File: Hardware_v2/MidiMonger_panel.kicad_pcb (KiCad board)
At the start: 2 copper layers, 40.3 x 128.5 mm, 32 parts

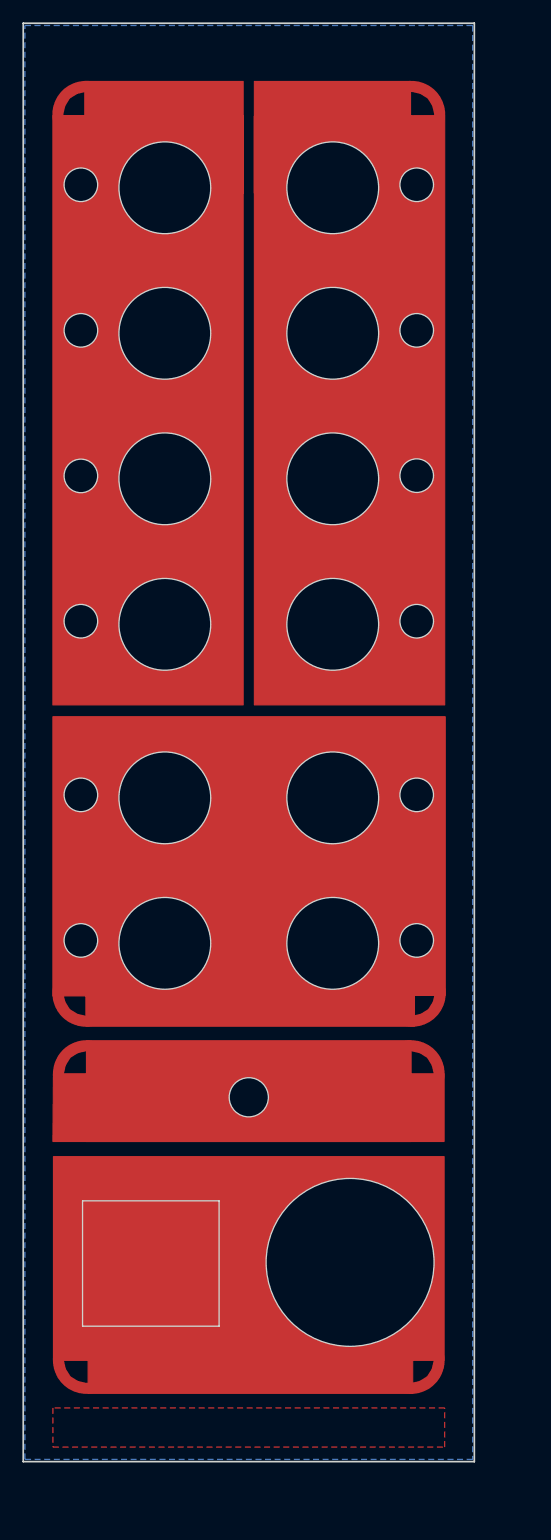
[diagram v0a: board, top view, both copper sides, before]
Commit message: Laying out panel
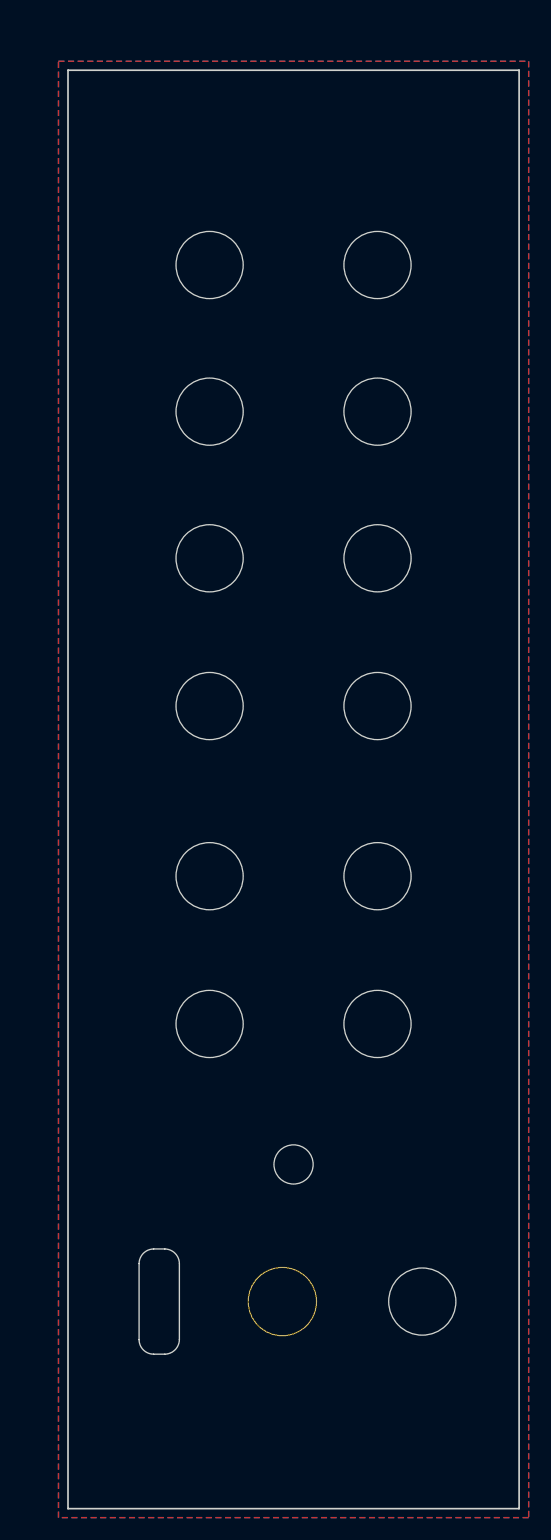
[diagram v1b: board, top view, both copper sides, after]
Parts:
- removed the Ref** at (123.5, 58.5)
- removed the Ref** at (123.5, 71.5)
- removed the Ref** at (123.5, 84.5)
- removed the Ref** at (123.5, 100.0)
- removed the Ref** at (123.5, 113.0)
- removed the Ref** at (108.5, 113.0)
- removed the Ref** at (108.5, 100.0)
- removed the Ref** at (108.5, 84.5)
- removed the Ref** at (108.5, 71.5)
- removed the Ref** at (108.5, 58.5)
- removed the Ref** at (108.5, 45.5)
- removed the Ref** at (123.5, 45.5)
- removed the Ref** at (125.0, 141.5)
- added REF**: USB_C_Cutout, Custom_Footprints:USB_C_Cutout, F.Cu at (108.0, 145.0)
- added Ref**: Thonkiconn_Socket_MountingHole_6mm, Custom_Footprints:Thonkiconn_Socket_MountingHole_6mm, F.Cu at (112.5, 52.4)
- added Ref**: Thonkiconn_Socket_MountingHole_6mm, Custom_Footprints:Thonkiconn_Socket_MountingHole_6mm, F.Cu at (112.5, 91.8)
- added Ref**: Thonkiconn_Socket_MountingHole_6mm, Custom_Footprints:Thonkiconn_Socket_MountingHole_6mm, F.Cu at (127.5, 78.6)
- added Ref**: Thonkiconn_Socket_MountingHole_6mm, Custom_Footprints:Thonkiconn_Socket_MountingHole_6mm, F.Cu at (127.5, 107.0)
- added Ref**: Thonkiconn_Socket_MountingHole_6mm, Custom_Footprints:Thonkiconn_Socket_MountingHole_6mm, F.Cu at (127.5, 65.5)
- added Ref**: Thonkiconn_Socket_MountingHole_6mm, Custom_Footprints:Thonkiconn_Socket_MountingHole_6mm, F.Cu at (127.5, 91.8)
- added Ref**: Thonkiconn_Socket_MountingHole_6mm, Custom_Footprints:Thonkiconn_Socket_MountingHole_6mm, F.Cu at (112.5, 78.6)
- added Ref**: Thonkiconn_Socket_MountingHole_6mm, Custom_Footprints:Thonkiconn_Socket_MountingHole_6mm, F.Cu at (131.5, 145.0)
- added Ref**: Thonkiconn_Socket_MountingHole_6mm, Custom_Footprints:Thonkiconn_Socket_MountingHole_6mm, F.Cu at (127.5, 120.2)
- added Ref**: Thonkiconn_Socket_MountingHole_6mm, Custom_Footprints:Thonkiconn_Socket_MountingHole_6mm, F.Cu at (112.5, 65.5)
- added Ref**: Subminiature_Switch, Custom_Footprints:DPDT_Switch_MountingHole_6mm, F.Cu at (119.0, 145.0)
- added Ref**: Thonkiconn_Socket_MountingHole_6mm, Custom_Footprints:Thonkiconn_Socket_MountingHole_6mm, F.Cu at (112.5, 107.0)
- added Ref**: Thonkiconn_Socket_MountingHole_6mm, Custom_Footprints:Thonkiconn_Socket_MountingHole_6mm, F.Cu at (127.5, 52.4)
- added Ref**: Thonkiconn_Socket_MountingHole_6mm, Custom_Footprints:Thonkiconn_Socket_MountingHole_6mm, F.Cu at (112.5, 120.2)
- added kibuzzard-66B25140: G***, kibuzzard-66B25140, F.Cu at (119.9, 113.6)
- added kibuzzard-66B25216: G***, kibuzzard-66B25216, F.Cu at (127.5, 44.7)
- added kibuzzard-66B252BB: G***, kibuzzard-66B252BB, F.Cu at (112.5, 44.7)
- added kibuzzard-66B25349: G***, kibuzzard-66B25349, F.Cu at (131.2, 152.0)
- Ref** (x12): footprint Custom_Footprints:Sub_Miniature_Switch_MountingHole_3mm -> Custom_Footprints:LED_Window
- moved Ref** 8.81 mm to (105.5, 91.8)
- moved Ref** 8.71 mm to (105.5, 120.2)
- moved Ref** 8.62 mm to (105.5, 78.6)
- moved Ref** 8.55 mm to (105.5, 107.0)
- moved Ref** 8.54 mm to (105.5, 65.5)
- moved Ref** 8.46 mm to (105.5, 52.4)
- moved Ref** 8.35 mm to (134.5, 91.8)
- moved Ref** 8.24 mm to (134.5, 120.2)
- moved Ref** 8.17 mm to (134.5, 78.6)
- moved Ref** 8.06 mm to (134.5, 107.0)
- moved Ref** 8.06 mm to (134.5, 65.5)
- moved Ref** 7.98 mm to (134.5, 52.4)
- moved G*** 7.28 mm to (129.1, 132.5)
- moved G*** 7.28 mm to (111.3, 131.5)
- moved Ref** 7.21 mm to (120.0, 132.8)
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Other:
- outline, holes or cut-outs redrawn
- net class Default removed
- board text removed: "CV/Pitch"
- board text removed: "Gate"

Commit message: Hardware layout
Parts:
- removed kibuzzard-66B25216: G***, kibuzzard-66B25216
- removed kibuzzard-66B252BB: G***, kibuzzard-66B252BB
- removed kibuzzard-66B25349: G***, kibuzzard-66B25349
- added G***: LOGO, Graphics:piano, F.Cu at (132.0, 153.4)
- added G***: LOGO, Graphics:computer, F.Cu at (132.1, 139.4)
- added kibuzzard-66B33BB1: G***, kibuzzard-66B33BB1, F.Cu at (129.3, 43.3)
- added kibuzzard-66B353F0: G***, kibuzzard-66B353F0, F.Cu at (110.5, 43.3)
- moved Ref** 23.2 mm to (108.3, 146.0)
- moved kibuzzard-66B25140 14.8 mm to (119.6, 128.4)
- moved Ref** 13.1 mm to (132.1, 146.0)
- moved REF** 12.0 mm to (120.0, 146.0)
- moved Ref** 2.05 mm to (120.1, 134.8)
- moved G*** 1.98 mm to (111.3, 133.4)
- moved G*** 1.98 mm to (129.1, 134.5)
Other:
- board text added: "MIDI"

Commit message: Gerbers prepared for manufacture
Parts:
- moved G*** 0.60 mm to (131.5, 139.4)
- moved Ref** 0.60 mm to (131.5, 146.0)
- moved G*** 0.50 mm to (131.5, 153.4)
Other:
- board text added: "Mountjoy Modular MIDI Monger Panel v2.0"
- board text added: "WayWayWay"
- board text removed: "JLCJLCJLCJLC"
- board text removed: "Mountjoy Modular MIDI Monger Panel v1.0"
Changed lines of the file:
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@@
 		(allow_soldermask_bridges_in_footprints no)
 		(pcbplotparams
-			(layerselection 0x00010fc_ffffffff)
+			(layerselection 0x00010f0_ffffffff)
 			(plot_on_all_layers_selection 0x0000000_00000000)
 			(disableapertmacros no)
@@
 				(font
 					(size 0.001 0.001)
+					(thickness 0.15)
 				)
 			)
@@
 				(font
 					(size 0.001 0.001)
+					(thickness 0.15)
 				)
 			)
@@
 	(footprint "Graphics:piano"
 		(layer "F.Cu")
-		(at 132 153.4)
+		(at 131.5 153.4)
 		(property "Reference" "G***"
 			(at 0 0 0)
@@
 				(font
 					(size 0.001 0.001)
+					(thickness 0.15)
 				)
 			)
@@
 				(font
 					(size 0.001 0.001)
+					(thickness 0.15)
 				)
 			)
@@
 				(font
 					(size 0.001 0.001)
+					(thickness 0.15)
 				)
 			)
@@
 				(font
 					(size 0.001 0.001)
+					(thickness 0.15)
 				)
 			)
@@
 	(footprint "Custom_Footprints:DPDT_Switch_MountingHole_6mm"
 		(layer "F.Cu")
-		(at 132.1 146)
+		(at 131.5 146)
 		(descr "Mounting Hole 6mm, no annular")
 		(tags "mounting hole 6mm no annular")
@@
 	(footprint "Graphics:computer"
 		(layer "F.Cu")
-		(at 132.1 139.4)
+		(at 131.5 139.4)
 		(property "Reference" "G***"
 			(at 0 0 0)
@@
 		(layer "Edge.Cuts")
 	)
-	(gr_text "Mountjoy Modular\nMIDI Monger Panel v1.0"
+	(gr_text "Mountjoy Modular\nMIDI Monger Panel v2.0"
 		(at 120.2 38 0)
 		(layer "B.SilkS")
@@
 		)
 	)
-	(gr_text "JLCJLCJLCJLC"
+	(gr_text "WayWayWay"
 		(at 119.9 160.5 0)
 		(layer "B.SilkS")

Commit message: Reversed MIDI device/host graphics on panel v2.1
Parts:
- moved G*** 14.0 mm to (131.5, 139.4)
- moved G*** 14.0 mm to (131.5, 153.4)
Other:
- board text added: "Mountjoy Modular MIDI Monger Panel v2.1"
- board text removed: "Mountjoy Modular MIDI Monger Panel v2.0"
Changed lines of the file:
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@@
 			(net 0)
 			(net_name "")
-			(layers "*.Cu")
+			(layers "F&B.Cu")
 			(name "LED_Window")
 			(hatch edge 0.5)
@@
 			(net 0)
 			(net_name "")
-			(layers "*.Cu")
+			(layers "F&B.Cu")
 			(name "LED_Window")
 			(hatch edge 0.5)
@@
 			(net 0)
 			(net_name "")
-			(layers "*.Cu")
+			(layers "F&B.Cu")
 			(name "LED_Window")
 			(hatch edge 0.5)
@@
 			(net 0)
 			(net_name "")
-			(layers "*.Cu")
+			(layers "F&B.Cu")
 			(name "LED_Window")
 			(hatch edge 0.5)
@@
 			(net 0)
 			(net_name "")
-			(layers "*.Cu")
+			(layers "F&B.Cu")
 			(name "LED_Window")
 			(hatch edge 0.5)
@@
 			(net 0)
 			(net_name "")
-			(layers "*.Cu")
+			(layers "F&B.Cu")
 			(name "LED_Window")
 			(hatch edge 0.5)
@@
 			(net 0)
 			(net_name "")
-			(layers "*.Cu")
+			(layers "F&B.Cu")
 			(name "LED_Window")
 			(hatch edge 0.5)
@@
 			(net 0)
 			(net_name "")
-			(layers "*.Cu")
+			(layers "F&B.Cu")
 			(name "LED_Window")
 			(hatch edge 0.5)
@@
 			(net 0)
 			(net_name "")
-			(layers "*.Cu")
+			(layers "F&B.Cu")
 			(name "LED_Window")
 			(hatch edge 0.5)
@@
 			(net 0)
 			(net_name "")
-			(layers "*.Cu")
+			(layers "F&B.Cu")
 			(name "LED_Window")
 			(hatch edge 0.5)
@@
 			(net 0)
 			(net_name "")
-			(layers "*.Cu")
+			(layers "F&B.Cu")
 			(name "LED_Window")
 			(hatch edge 0.5)
@@
 			(net 0)
 			(net_name "")
-			(layers "*.Cu")
+			(layers "F&B.Cu")
 			(name "LED_Window")
 			(hatch edge 0.5)
@@
 	(footprint "Graphics:piano"
 		(layer "F.Cu")
-		(at 131.5 153.4)
+		(at 131.5 139.4)
 		(property "Reference" "G***"
 			(at 0 0 0)
@@
 	(footprint "Graphics:computer"
 		(layer "F.Cu")
-		(at 131.5 139.4)
+		(at 131.5 153.4)
 		(property "Reference" "G***"
 			(at 0 0 0)
@@
 		(layer "Edge.Cuts")
 	)
-	(gr_text "Mountjoy Modular\nMIDI Monger Panel v2.0"
+	(gr_text "Mountjoy Modular\nMIDI Monger Panel v2.1"
 		(at 120.2 38 0)
 		(layer "B.SilkS")
